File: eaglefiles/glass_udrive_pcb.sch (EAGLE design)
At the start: 23 parts

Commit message: updated several board layout details: made it smaller H and W, changed the anchoring tab on the opposite side, added +-15 power supply pours to simplify routing and reduced bridge resistor size to 408 package 1/16 W 100Mohm resistor.
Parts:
- BRIDGE: device GFL:R_1206 -> GFL:R_0402
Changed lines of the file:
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@@
 <part name="FRAME1" library="frames" deviceset="LETTER_L" device=""/>
 <part name="OMNETICS" library="GFL" deviceset="OMNETICS_A75243-001" device=""/>
-<part name="BRIDGE" library="GFL" deviceset="R" device="_1206" value="100MOhm"/>
+<part name="BRIDGE" library="GFL" deviceset="R" device="_0402" value="100MOhm"/>
 <part name="CAPCOM" library="GFL" deviceset="C" device="_0402" value="10pF"/>
 <part name="C1" library="GFL" deviceset="C" device="_0201" value="0.1uF"/>

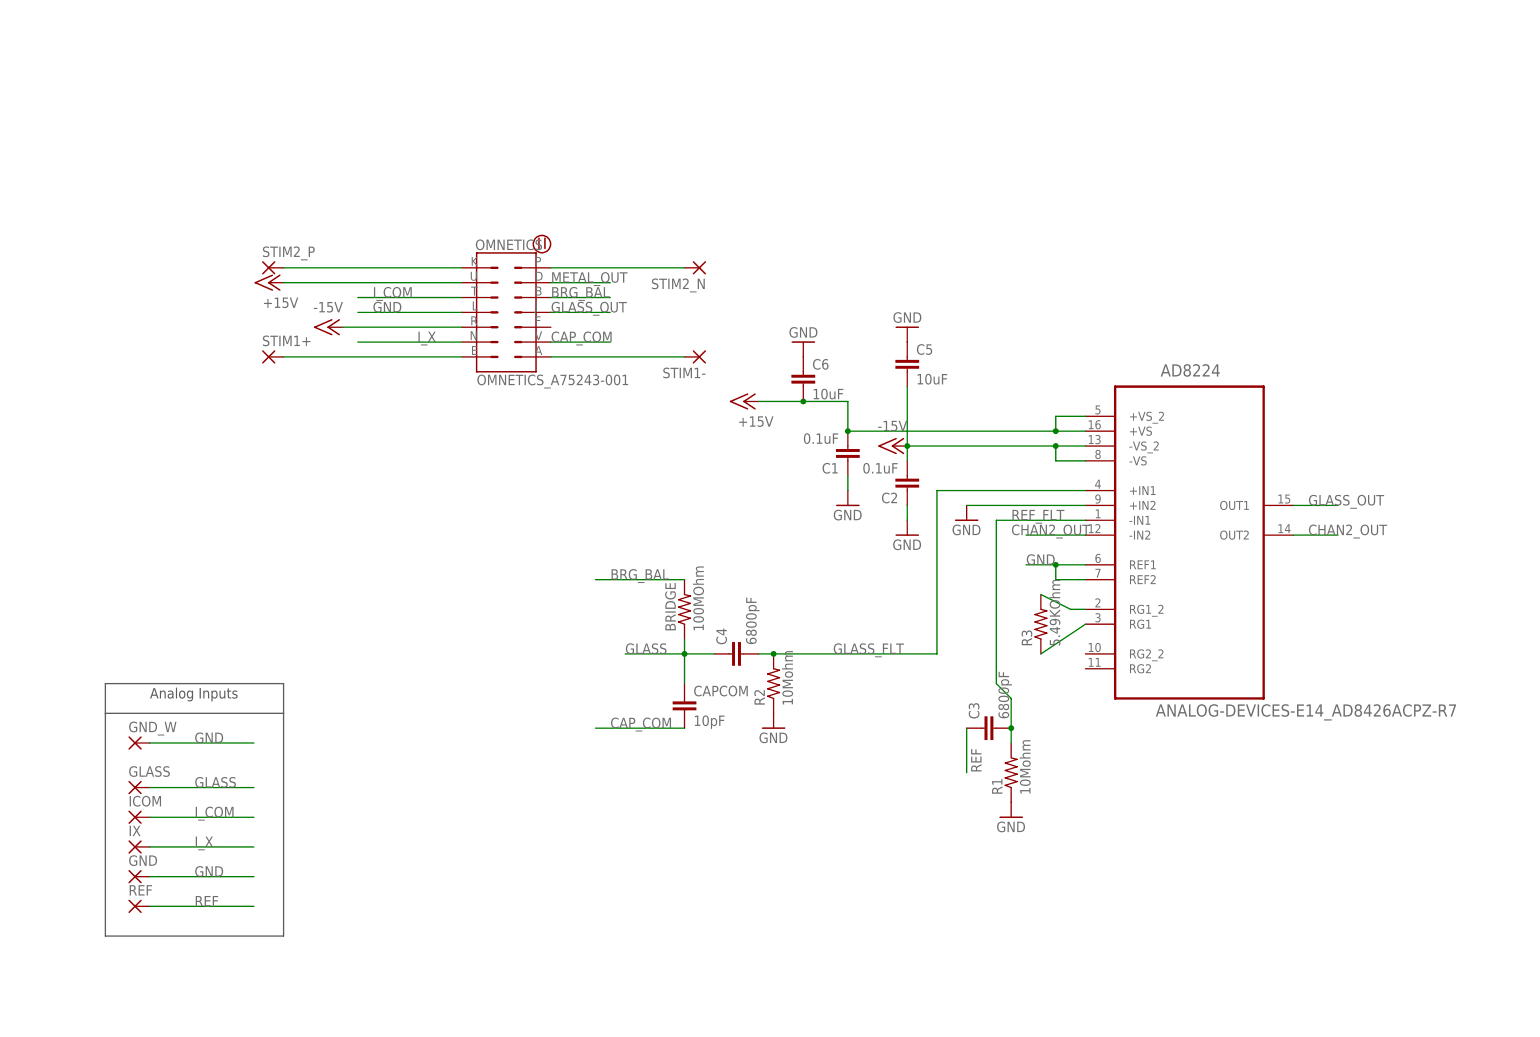
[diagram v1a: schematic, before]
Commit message: Added optional circuit for 2nd INA channel and routing optimized.
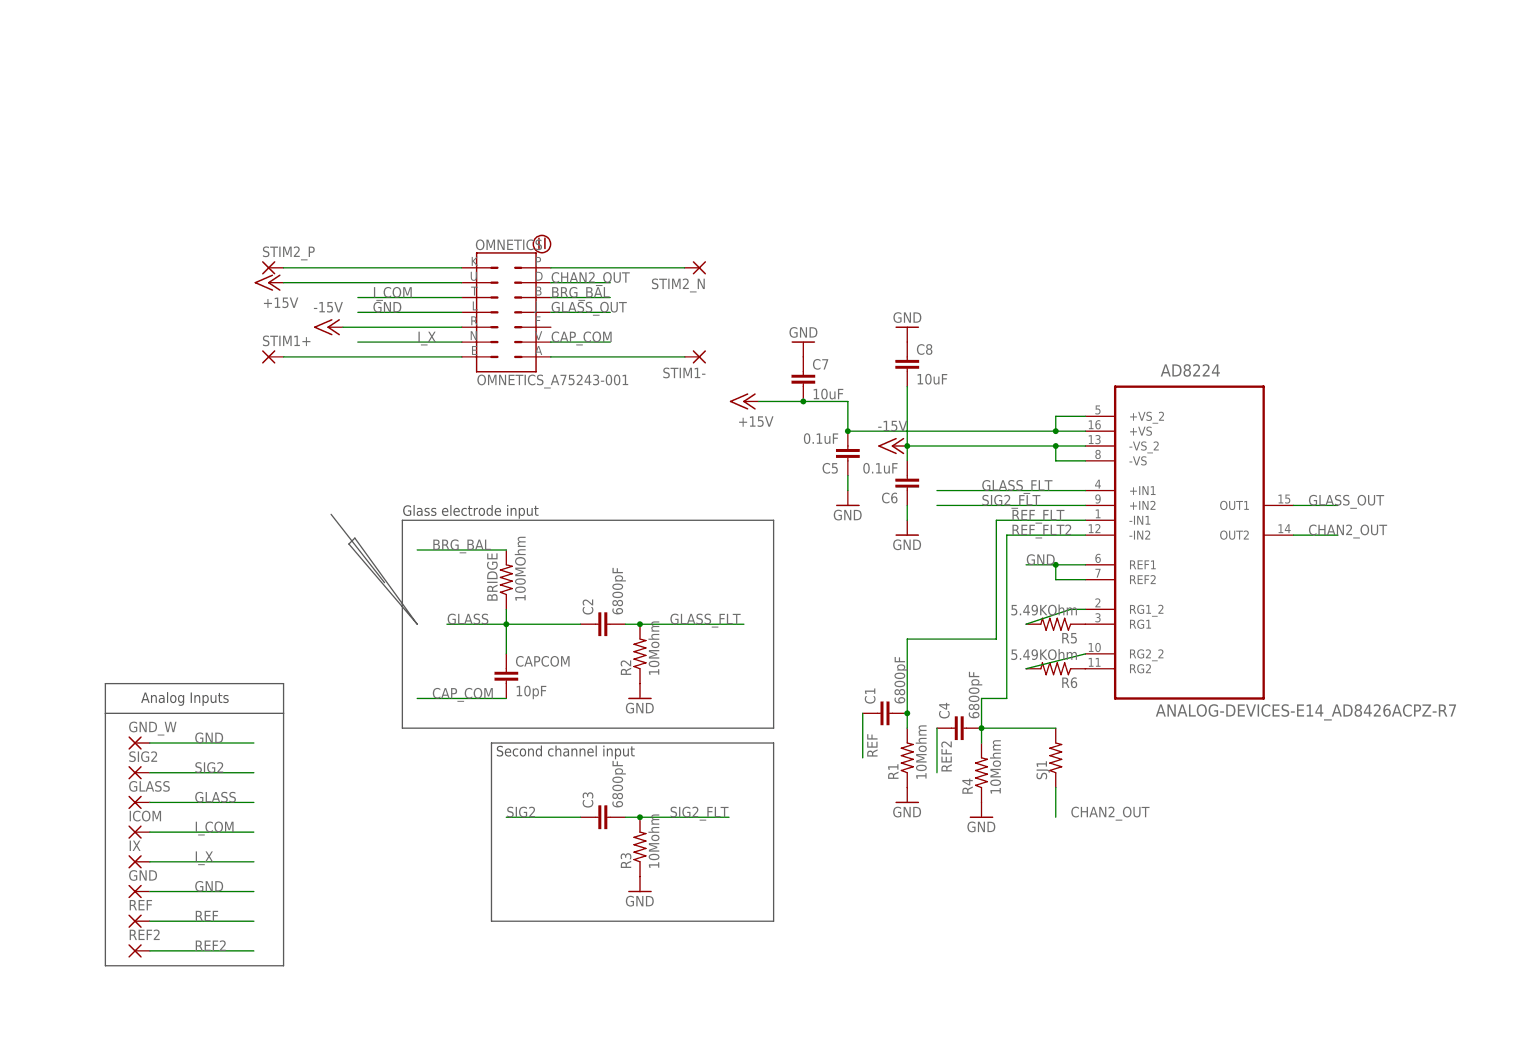
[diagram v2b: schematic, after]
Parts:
- added C7, C8: 10uF, GFL:C_0603
- added R4: 10Mohm, GFL:R_0201
- added R5, R6: 5.49KOhm, GFL:R_0201
- added REF2, SIG2: (no value), GFL:THROUGH-HOLE-30MIL/15MIL
- added SJ1: (no value), GFL:R_0201
- C1, C2: value 0.1uF -> 6800pF
- C5, C6: value 10uF -> 0.1uF; device GFL:C_0603 -> GFL:C_0201
- R3: value 5.49KOhm -> 10Mohm
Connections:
- removed net METAL_OUT: OMNETICS.D
- new net N$6: AD8224.RG2_2, R6.2
- new net N$7: AD8224.RG2, R6.1
- new net REF2: C4.1, REF2.P
- new net REF_FLT2: AD8224.-IN2, C4.2, R4.2, SJ1.2
- new net SIG2: C3.1, SIG2.P
- new net SIG2_FLT: AD8224.+IN2, C3.2, R3.2
- net +15V: now also C5.2, C7.2; no longer C1.2, C6.2
- net -15V: now also C6.2, C8.2; no longer C2.2, C5.2
- net CHAN2_OUT: now also OMNETICS.D, SJ1.1; no longer AD8224.-IN2
- net GLASS: now also C2.1; no longer C4.1
- net GLASS_FLT: now also C2.2; no longer C4.2
- net GND: now also C7.1, C8.1, R3.1, R4.1; no longer AD8224.+IN2, C1.1, C2.1
- net N$2: now also R5.2; no longer R3.2
- net N$4: now also R5.1; no longer R3.1
- net REF: now also C1.1; no longer C3.1
- net REF_FLT: now also C1.2; no longer C3.2
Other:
- note added: "Glass electrode input"
- note added: "Second channel input"
- moved on the sheet: BRIDGE, C1, C2, C3, C4, C5, C6, CAPCOM, GLASS, GND, ICOM, IX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

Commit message: Went very OCD on your design
Made the power planes bigger because they had no reason not to be.

Renamed some nets because I found them confusing when looking at your schematic.

Moved stuff for cleaner routing.

Added a top ground plane to prevent stray capacitance onto any moving wires for
your electrode etc.

Improved via placement on bypass capacitors.

Re-organized schematic to some degree.

Renamed components to have more standard designator names, e.g. P1 instead of
'omnetics' and U1 instead of "AD82**"

Moved vias around to not make big breaks in the ground plane.

Messed with dimensions so they're all rectilinear and meet up with eachother.
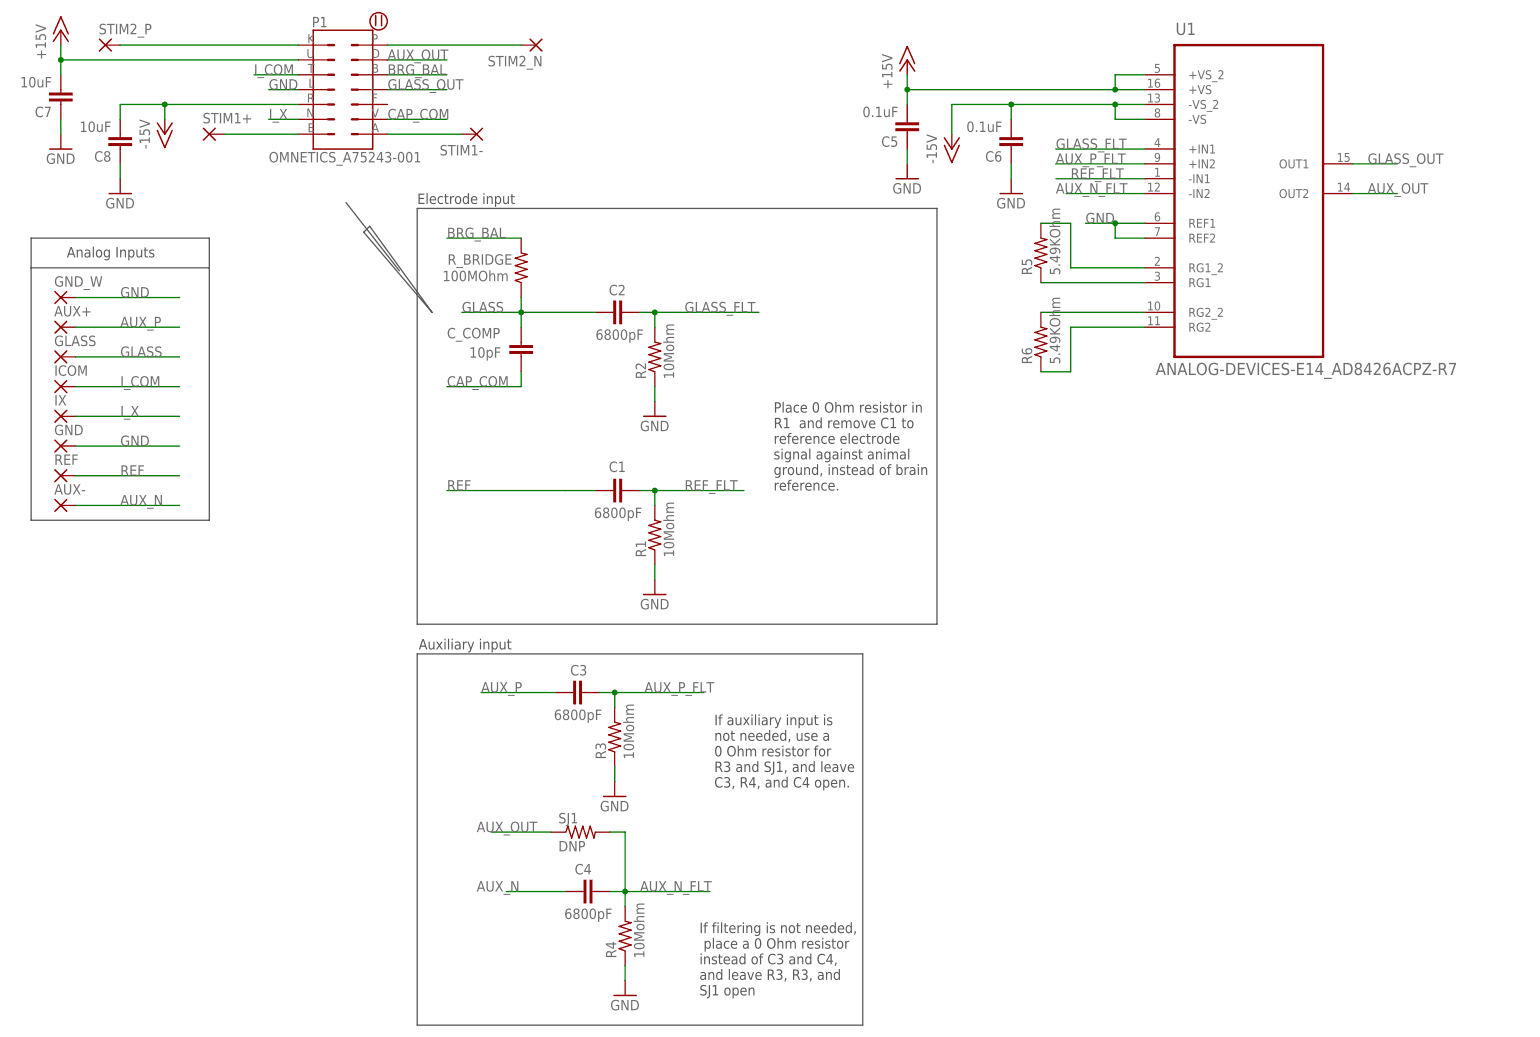
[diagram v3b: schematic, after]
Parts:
- removed AD8224: ANALOG-DEVICES-E14_AD8426ACPZ-R7, GyroDrive:ANALOG-DEVICES-E14_AD8426ACPZ-R7
- removed BRIDGE: 100MOhm, GFL:R_0402
- removed CAPCOM: 10pF, GFL:C_0402
- removed OMNETICS: OMNETICS_A75243-001, GFL:OMNETICS_A75243-001
- removed REF2, SIG2: (no value), GFL:THROUGH-HOLE-30MIL/15MIL
- added AUX+, AUX-: (no value), GFL:THROUGH-HOLE-30MIL/15MIL
- added C_COMP: 10pF, GFL:C_0402
- added P1: OMNETICS_A75243-001, GFL:OMNETICS_A75243-001
- added R_BRIDGE: 100MOhm, GFL:R_0402
- added U1: ANALOG-DEVICES-E14_AD8426ACPZ-R7, GyroDrive:ANALOG-DEVICES-E14_AD8426ACPZ-R7
- SJ1: value (none) -> DNP
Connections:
- removed net CHAN2_OUT: AD8224.OUT2, OMNETICS.D, SJ1.1
- removed net REF2: C4.1, REF2.P
- removed net REF_FLT2: AD8224.-IN2, C4.2, R4.2, SJ1.2
- removed net SIG2: C3.1, SIG2.P
- removed net SIG2_FLT: AD8224.+IN2, C3.2, R3.2
- new net AUX_N: AUX-.P, C4.1
- new net AUX_N_FLT: C4.2, R4.2, SJ1.2, U1.-IN2
- new net AUX_OUT: P1.D, SJ1.1, U1.OUT2
- new net AUX_P: AUX+.P, C3.1
- new net AUX_P_FLT: C3.2, R3.2, U1.+IN2
- net +15V: now also P1.U, U1.+VS, U1.+VS_2; no longer AD8224.+VS, AD8224.+VS_2, OMNETICS.U
- net -15V: now also P1.R, U1.-VS, U1.-VS_2; no longer AD8224.-VS, AD8224.-VS_2, OMNETICS.R
- net BRG_BAL: now also P1.B, R_BRIDGE.2; no longer BRIDGE.2, OMNETICS.B
- net CAP_COM: now also C_COMP.2, P1.V; no longer CAPCOM.2, OMNETICS.V
- net GLASS: now also C_COMP.1, R_BRIDGE.1; no longer BRIDGE.1, CAPCOM.1
- net GLASS_FLT: now also U1.+IN1; no longer AD8224.+IN1
- net GLASS_OUT: now also P1.J, U1.OUT1; no longer AD8224.OUT1, OMNETICS.J
- net GND: now also P1.L, U1.REF1, U1.REF2; no longer AD8224.REF1, AD8224.REF2, OMNETICS.L
- net I_COM: now also P1.T; no longer OMNETICS.T
- net I_X: now also P1.N; no longer OMNETICS.N
- net N$2: now also U1.RG1_2; no longer AD8224.RG1_2
- net N$4: now also U1.RG1; no longer AD8224.RG1
- net N$6: now also U1.RG2_2; no longer AD8224.RG2_2
- net N$7: now also U1.RG2; no longer AD8224.RG2
- net REF_FLT: now also U1.-IN1; no longer AD8224.-IN1
- net STIM1_N: now also P1.A; no longer OMNETICS.A
- net STIM1_P: now also P1.E; no longer OMNETICS.E
- net STIM2_N: now also P1.P; no longer OMNETICS.P
- net STIM2_P: now also P1.K; no longer OMNETICS.K
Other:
- note added: "Auxiliary input"
- note added: "Electrode input"
- note added: "If auxiliary input is not needed, use a 0 Ohm resistor for R3 and SJ1, and leave C3, R4, and C4 open."
- note added: "If filtering is not needed, place a 0 Ohm resistor instead of C3 and C4, and leave R3, R3, and SJ1 open"
- note added: "Place 0 Ohm resistor in R1 and remove C1 to reference electrode signal against animal ground, instead of brain reference."
- note removed: "Glass electrode input"
- note removed: "Second channel input"
- moved on the sheet: C1, C2, C3, C4, C5, C6, C7, C8, GLASS, GND, GND_W, ICOM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

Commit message: Made glass net more compact.
Silk screen needs a lot of work
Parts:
- renumbered GND to G, REF to R, STIM2_N to S2+, STIM2_P to S2-
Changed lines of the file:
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@@
 <part name="P-2" library="supply1" deviceset="-15V" device=""/>
 <part name="GLASS" library="GFL" deviceset="THROUGH-HOLE-30MIL/15MIL" device=""/>
-<part name="STIM2_N" library="GFL" deviceset="THROUGH-HOLE-30MIL/15MIL" device=""/>
+<part name="S2+" library="GFL" deviceset="THROUGH-HOLE-30MIL/15MIL" device=""/>
 <part name="IX" library="GFL" deviceset="THROUGH-HOLE-30MIL/15MIL" device=""/>
 <part name="STIM1-" library="GFL" deviceset="THROUGH-HOLE-30MIL/15MIL" device=""/>
 <part name="STIM1+" library="GFL" deviceset="THROUGH-HOLE-30MIL/15MIL" device=""/>
-<part name="STIM2_P" library="GFL" deviceset="THROUGH-HOLE-30MIL/15MIL" device=""/>
+<part name="S2-" library="GFL" deviceset="THROUGH-HOLE-30MIL/15MIL" device=""/>
 <part name="ICOM" library="GFL" deviceset="THROUGH-HOLE-30MIL/15MIL" device=""/>
-<part name="GND" library="GFL" deviceset="THROUGH-HOLE-30MIL/15MIL" device=""/>
+<part name="G" library="GFL" deviceset="THROUGH-HOLE-30MIL/15MIL" device=""/>
 <part name="U1" library="GyroDrive" deviceset="ANALOG-DEVICES-E14_AD8426ACPZ-R7" device=""/>
-<part name="REF" library="GFL" deviceset="THROUGH-HOLE-30MIL/15MIL" device=""/>
+<part name="R" library="GFL" deviceset="THROUGH-HOLE-30MIL/15MIL" device=""/>
 <part name="R5" library="GFL" deviceset="R" device="_0201" value="5.49KOhm"/>
 <part name="R2" library="GFL" deviceset="R" device="_0201" value="10Mohm"/>
@@
 <instance part="P-2" gate="1" x="0" y="147.32"/>
 <instance part="GLASS" gate="P" x="-17.78" y="109.22"/>
-<instance part="STIM2_N" gate="P" x="63.5" y="162.56" rot="R180"/>
+<instance part="S2+" gate="P" x="63.5" y="162.56" rot="R180"/>
 <instance part="IX" gate="P" x="-17.78" y="99.06"/>
 <instance part="STIM1-" gate="P" x="53.34" y="147.32" rot="R180"/>
 <instance part="STIM1+" gate="P" x="7.62" y="147.32"/>
-<instance part="STIM2_P" gate="P" x="-10.16" y="162.56"/>
+<instance part="S2-" gate="P" x="-10.16" y="162.56"/>
 <instance part="ICOM" gate="P" x="-17.78" y="104.14"/>
-<instance part="GND" gate="P" x="-17.78" y="93.98"/>
+<instance part="G" gate="P" x="-17.78" y="93.98"/>
 <instance part="U1" gate="A" x="185.42" y="139.7" smashed="yes">
 <attribute name="NAME" x="172.8724" y="164.2872" size="2.0828" layer="95" ratio="10" rot="SR0"/>
 <attribute name="VALUE" x="169.4942" y="106.1212" size="2.0828" layer="96" ratio="10" rot="SR0"/>
 </instance>
-<instance part="REF" gate="P" x="-17.78" y="88.9"/>
+<instance part="R" gate="P" x="-17.78" y="88.9"/>
 <instance part="R5" gate="R" x="149.86" y="127" rot="R90"/>
 <instance part="R2" gate="R" x="83.82" y="109.22" rot="R90"/>
@@
 <wire x1="-15.24" y1="93.98" x2="2.54" y2="93.98" width="0.1524" layer="91"/>
 <label x="-7.62" y="93.98" size="1.778" layer="95"/>
-<pinref part="GND" gate="P" pin="P"/>
+<pinref part="G" gate="P" pin="P"/>
 </segment>
 <segment>
@@
 <pinref part="P1" gate="G$1" pin="P"/>
 <wire x1="60.96" y1="162.56" x2="38.1" y2="162.56" width="0.1524" layer="91"/>
-<pinref part="STIM2_N" gate="P" pin="P"/>
+<pinref part="S2+" gate="P" pin="P"/>
 </segment>
 </net>
@@
 <segment>
 <pinref part="P1" gate="G$1" pin="K"/>
-<pinref part="STIM2_P" gate="P" pin="P"/>
+<pinref part="S2-" gate="P" pin="P"/>
 <wire x1="22.86" y1="162.56" x2="-7.62" y2="162.56" width="0.1524" layer="91"/>
 </segment>
@@
 <net name="REF" class="0">
 <segment>
-<pinref part="REF" gate="P" pin="P"/>
+<pinref part="R" gate="P" pin="P"/>
 <wire x1="-15.24" y1="88.9" x2="2.54" y2="88.9" width="0.1524" layer="91"/>
 <label x="-7.62" y="88.9" size="1.778" layer="95"/>

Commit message: improvements on slikscreen and component naming and placing.
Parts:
- renumbered GND_W to G_W
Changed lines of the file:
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@@
 <part name="C8" library="GFL" deviceset="C" device="_0603" value="10uF"/>
 <part name="GND7" library="supply1" deviceset="GND" device=""/>
-<part name="GND_W" library="GFL" deviceset="THROUGH-HOLE-30MIL/15MIL" device=""/>
+<part name="G_W" library="GFL" deviceset="THROUGH-HOLE-30MIL/15MIL" device=""/>
 <part name="AUX+" library="GFL" deviceset="THROUGH-HOLE-30MIL/15MIL" device=""/>
 <part name="R4" library="GFL" deviceset="R" device="_0201" value="10Mohm"/>
@@
 <instance part="C8" gate="C" x="-7.62" y="144.78" rot="R180"/>
 <instance part="GND7" gate="1" x="-7.62" y="137.16"/>
-<instance part="GND_W" gate="P" x="-17.78" y="119.38"/>
+<instance part="G_W" gate="P" x="-17.78" y="119.38"/>
 <instance part="AUX+" gate="P" x="-17.78" y="114.3"/>
 <instance part="R4" gate="R" x="78.74" y="10.16" rot="R90"/>
@@
 </segment>
 <segment>
-<pinref part="GND_W" gate="P" pin="P"/>
+<pinref part="G_W" gate="P" pin="P"/>
 <wire x1="-15.24" y1="119.38" x2="2.54" y2="119.38" width="0.1524" layer="91"/>
 <label x="-7.62" y="119.38" size="1.778" layer="95"/>
